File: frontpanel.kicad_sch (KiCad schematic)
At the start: 33 parts, among them J11 OLED_SOG320132A_M383, J12 Stemma-QT_QWIIC, M3 Pico_Display_Pack, Q6 Si2306BDS, SW1 STOP_SW, SW2 Rotary Enc EC11E, U10 MCP23017_SO, U14 DS3231

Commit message: More updates to regularise property names
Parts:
- BT2: Manuf (none) -> Keystone; Manuf Part No 500 -> (none); Manufacturer Keystone -> (none); Mfr Keystone Elec. -> (none); Mfr Part No 500 -> (none); Part (none) -> 500; Supl Mouser -> (none); Supl Part No 534-500 -> (none); Supl Price 1.23 -> (none); Supplier Mouser -> (none); Vendor (none) -> Mouser; Vendor Cost (none) -> 1.23; Vendor SKU (none) -> 534-500
- C24, C35, C36, C37, C38, C51: Manuf (none) -> Samsung Electro-Mechanics; Mfr Samsung Electro-Mechanics -> (none); Mfr Name C0402C104K8R7411 -> (none); Mfr Part Mouser -> (none); Mfr Part No CL21B104KACNNND -> (none); Part 0.016 -> CL21B104KACNNND; Price KEMET -> (none); Repr-Cost C0402C104K8R7411 -> (none); Stock Number Mouser -> (none); Supl Mouser -> (none); Supl Part No 187-CL21B104KACNNND -> (none); Supl Price 0.027 -> (none); Vendor (none) -> Mouser; Vendor Cost (none) -> 0.027; Vendor SKU (none) -> 187-CL21B104KACNNND
- D14: Cost 1.37 -> (none); Manuf (none) -> kingbright; Manuf Part No WP154A4SUREQBFZG -> (none); Manufacturer kingbright -> (none); Part (none) -> WP154A4SUREQBFZG; Supplier mouser -> (none); Vendor (none) -> Mouser; Vendor Cost (none) -> 1.37; Vendor SKU (none) -> WP154A4SUREQBFZG
- J11: Manuf (none) -> Surenoo; Mfr Surenoo -> (none); Mfr Part No SOG320132A_M383 -> (none); Part (none) -> SOG320132A_M383
- M3: Manuf (none) -> ThePiHut; Mfr ThePiHut -> (none)
- Q6: Manuf (none) -> Vishay; Mfr Vishay -> (none); Mfr Part No SI2306BDS-T1-E3 -> (none); Part (none) -> SI2306BDS-T1-E3; Supl Mouser -> (none); Supl Part No 781-SI2306BDS-E3 -> (none); Supl Price 0.496 -> (none); Vendor (none) -> Mouser; Vendor Cost (none) -> 0.496; Vendor SKU (none) -> 781-SI2306BDS-E3
- R23, R24, R47, R48, R49: Manuf (none) -> Yageo; Mfr Yageo -> (none); Mfr Part No RC0805FR-134K7L -> (none); Part (none) -> RC0805FR-134K7L; Supl Mouser -> (none); Supl Part No 603-RC0805FR-134K7L -> (none); Supl Price 0.077 -> (none); Vendor (none) -> Mouser; Vendor Cost (none) -> 0.077; Vendor SKU (none) -> 603-RC0805FR-134K7L
- R25, R26, R27, R28, R29: Manuf (none) -> Yageo; Mfr Yageo -> (none); Mfr Part No AC0805FR-0710KL -> (none); Part (none) -> AC0805FR-0710KL; Supl Mouser -> (none); Supl Part No 603-AC0805FR-0710KL -> (none); Supl Price 0.077 -> (none); Vendor (none) -> Mouser; Vendor Cost (none) -> 0.077; Vendor SKU (none) -> 603-AC0805FR-0710KL
- SW1: Manuf (none) -> Schurter; Mfr Schurter -> (none); Mfr Part No 1241.1082.1 -> (none); Part (none) -> 1241.1082.1; Supl Mouser -> (none); Supl Part No 693-1241.1082.1 -> (none); Supl Price 3.07 -> (none); Vendor (none) -> Mouser; Vendor Cost (none) -> 3.07; Vendor SKU (none) -> 693-1241.1082.1
- SW2: Manuf (none) -> Alps; Mfr Alps -> (none); Mfr Part No EC11E152U402 -> (none); Part (none) -> EC11E152U402; Supl Mouser -> (none); Supl Part No 688-EC11E152U402 -> (none); Supl Price 11.34 -> (none); Vendor (none) -> Mouser; Vendor Cost (none) -> 11.34; Vendor SKU (none) -> 688-EC11E152U402
- U10: Manuf (none) -> Microchip; Mfr Microchip -> (none); Mfr Part No MCP23017-E/SO -> (none); Part (none) -> MCP23017-E/SO; Supl Mouser -> (none); Supl Part No 579-MCP23017-E/SO -> (none); Supl Price 1.13 -> (none); Vendor (none) -> Mouser; Vendor Cost (none) -> 1.13; Vendor SKU (none) -> 579-MCP23017-E/SO
- U14: Manuf (none) -> Maxim; Manuf Part No DS3231S#T&R -> (none); Manufacturer Maxim Integrated -> (none); Mfr Maxim -> (none); Mfr Part No DS3231 -> (none); Part (none) -> DS3231; Stock Number 700-DS3231S#T&R- -> (none); Supplier Mouser -> (none)

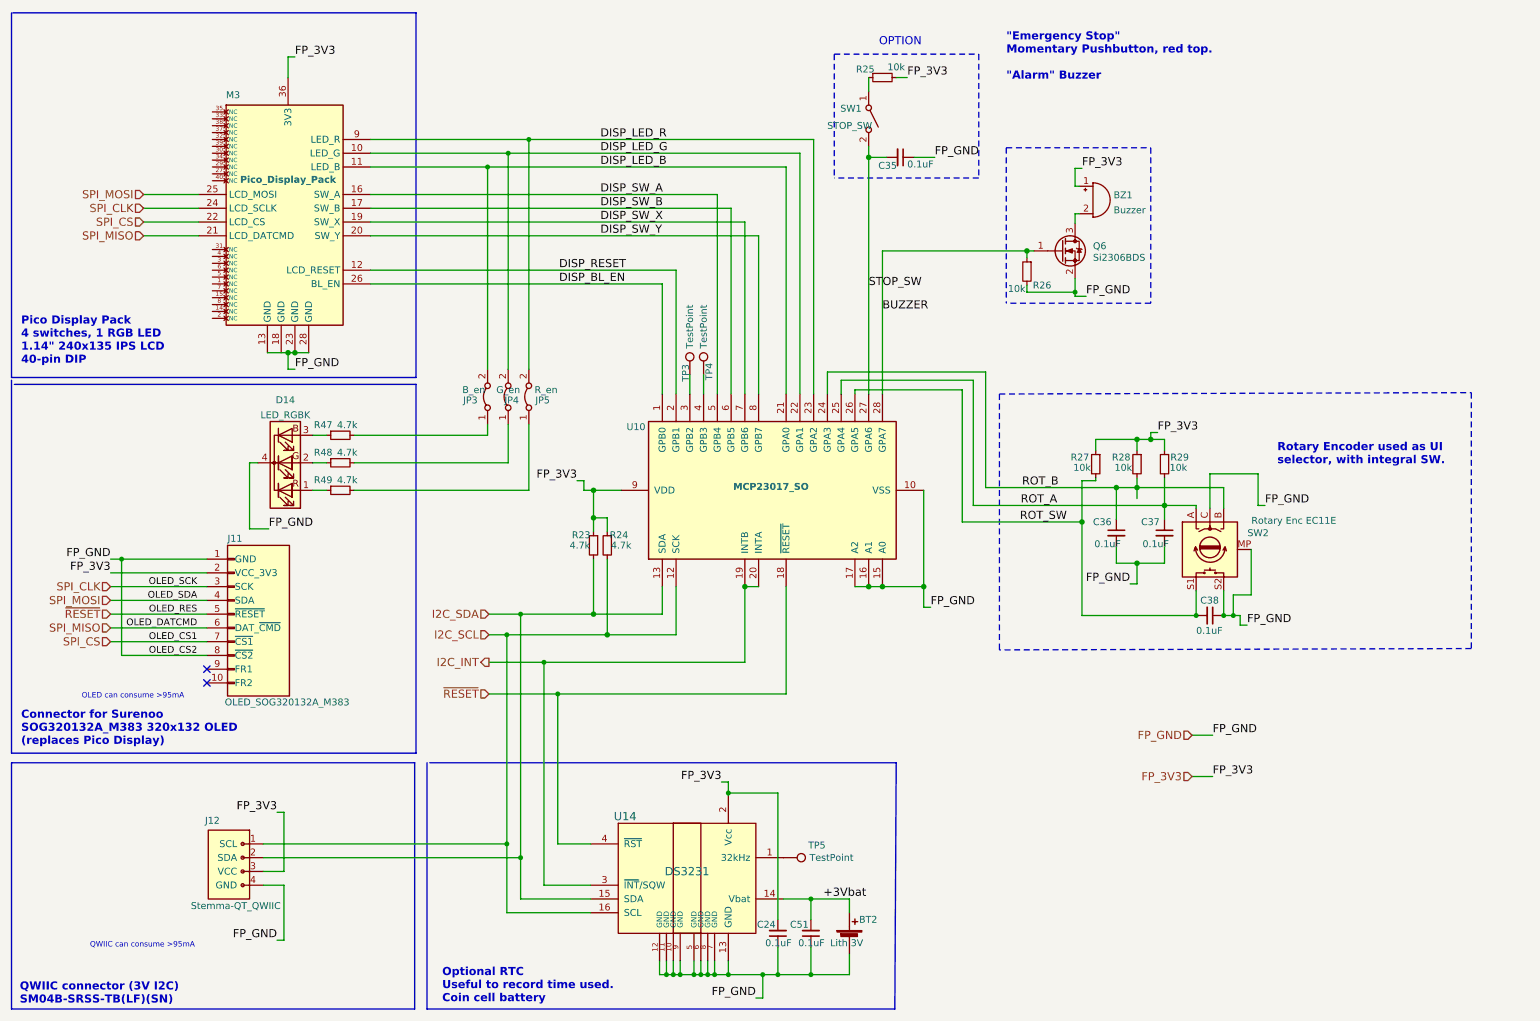
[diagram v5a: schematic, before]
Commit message: Fix some errors in the design (esp net-tie in wrong place)
 - correct led, diode footprints & model
 - fix fuse holder (bad hole spec)
 - update oled mod
 - update EC11 mod
 - add Blender models of case (xz compressed)
 - more updated gerbers (not current!)
 - improve layout of front panel pcb
 - delete unused files
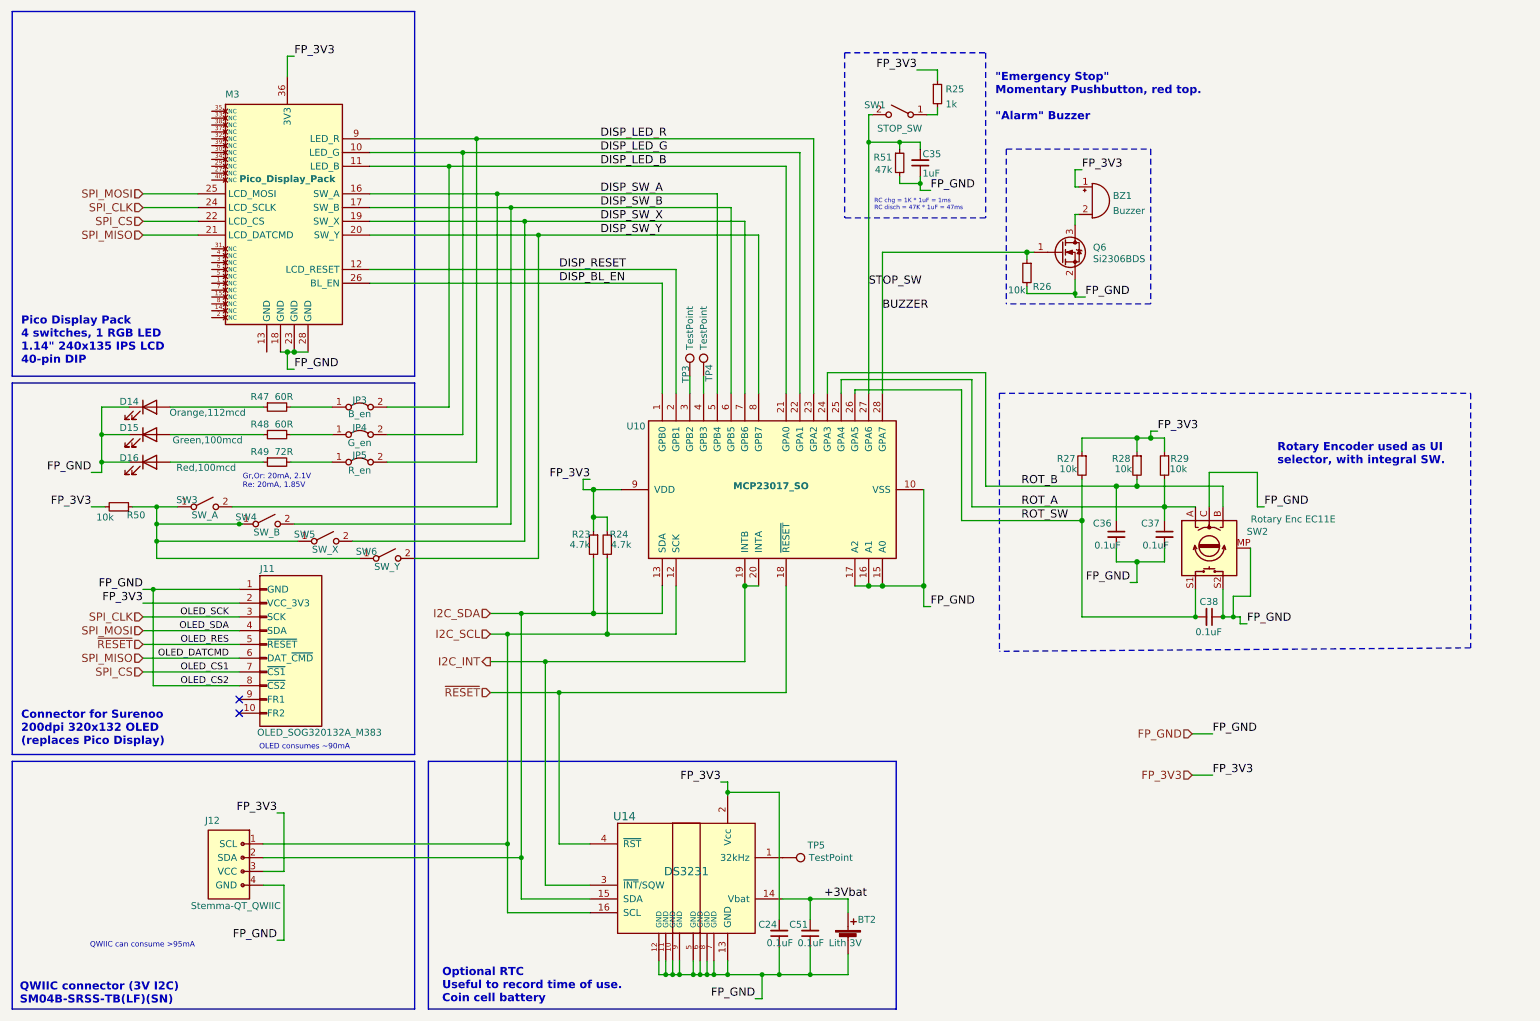
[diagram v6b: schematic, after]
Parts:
- removed D14: LED_RGBK, LED_THT:LED_D5.0mm-4_RGB_Wide_Pins, symbol Device:LED_RGBK
- added D14: Orange,112mcd, LED_SMD:LED_1206_3216Metric_Pad1.42x1.75mm_HandSolder, symbol Device:LED
- added D15: Green,100mcd, LED_SMD:LED_1210_3225Metric_Pad1.42x2.65mm_HandSolder, symbol Device:LED
- added D16: Red,100mcd, LED_SMD:LED_1206_3216Metric_Pad1.42x1.75mm_HandSolder, symbol Device:LED
- added R50: 10k, Resistor_SMD:R_0805_2012Metric_Pad1.20x1.40mm_HandSolder, symbol Device:R_Small
- added R51: 47k, Resistor_SMD:R_0805_2012Metric_Pad1.20x1.40mm_HandSolder, symbol Device:R_Small
- added SW3: SW_A, Connector_Wire:SolderWire-0.5sqmm_1x02_P4.6mm_D0.9mm_OD2.1mm, symbol Switch:SW_SPST
- added SW4: SW_B, Connector_Wire:SolderWire-0.5sqmm_1x02_P4.6mm_D0.9mm_OD2.1mm, symbol Switch:SW_SPST
- added SW5: SW_X, Connector_Wire:SolderWire-0.5sqmm_1x02_P4.6mm_D0.9mm_OD2.1mm, symbol Switch:SW_SPST
- added SW6: SW_Y, Connector_Wire:SolderWire-0.5sqmm_1x02_P4.6mm_D0.9mm_OD2.1mm, symbol Switch:SW_SPST
- C35: value 0.1uF -> 1uF; Manuf Samsung Electro-Mechanics -> Taiyo Yuden; Part CL21B104KACNNND -> EMK212BJ105KG-T; Vendor Cost 0.027 -> 0.016; Vendor SKU 187-CL21B104KACNNND -> 963-EMK212BJ105KG-T
- J11: Vendor (none) -> Surenoo; Vendor Cost (none) -> 39.95; Vendor SKU (none) -> SOG320132A_M383
- J12: Manuf (none) -> SparkFun; Part (none) -> PRT-14417; Vendor (none) -> Mouser; Vendor Cost (none) -> 0.399; Vendor SKU (none) -> 474-PRT-14417
- R25: value 10k -> 1k; Part AC0805FR-0710KL -> RC0805FR-071KL; Vendor SKU 603-AC0805FR-0710KL -> 603-RC0805FR-071KL
- R47, R48: value 4.7k -> 60R; Manuf Yageo -> Vishay / Dale; Part RC0805FR-134K7L -> CRCW080562R0JNEA; Vendor SKU 603-RC0805FR-134K7L -> 71-CRCW080562R0JNEA
- R49: value 4.7k -> 72R; Part RC0805FR-134K7L -> RC0805JR-0768RL; Vendor SKU 603-RC0805FR-134K7L -> 603-RC0805JR-0768RL
- U14: Vendor (none) -> Mouser; Vendor Cost (none) -> 7.39; Vendor SKU (none) -> 700-DS3231M+TRL
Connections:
- net DISP_SW_A: now also SW3.2 (B)
- net DISP_SW_B: now also SW4.2 (B)
- net DISP_SW_X: now also SW5.2 (B)
- net DISP_SW_Y: now also SW6.2 (B)
- net FP_3V3: now also R25.1, R50.2; no longer R25.2
- net FP_GND: now also M3.18 (GND), D14.1 (K), D15.1 (K), D16.1 (K), R51.2; no longer M3.13 (GND)
- net STOP_SW: now also R51.1
- net at R49.1: now also D16.2 (A)
- net at R47.1: now also D14.2 (A)
- net at R48.1: now also D15.2 (A)
- net at SW1.1 (A): now also R25.2; no longer R25.1
- new net: R50.1, SW3.1 (A), SW4.1 (A), SW5.1 (A), SW6.1 (A)
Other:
- note added: "Connector for Surenoo 200dpi 320x132 OLED (replaces Pico Display)"
- note added: "Gr,Or: 20mA, 2.1V Re: 20mA, 1.85V"
- note added: "OLED consumes ~90mA"
- note added: "Optional RTC Useful to record time of use. Coin cell battery"
- note added: "RC chg = 1K * 1uF = 1ms RC disch = 47K * 1uF = 47ms"
- note removed: "Connector for Surenoo SOG320132A_M383 320x132 OLED (replaces Pico Display)"
- note removed: "OLED can consume >95mA"
- note removed: "OPTION"
- note removed: "Optional RTC Useful to record time used. Coin cell battery"
- moved on the sheet: J11, JP3, JP4, JP5, R27, R47, R48, R49, SW1

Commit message: Adjust to supply 2 CS sigs to display; rename MISO to DC; larger conn cable.
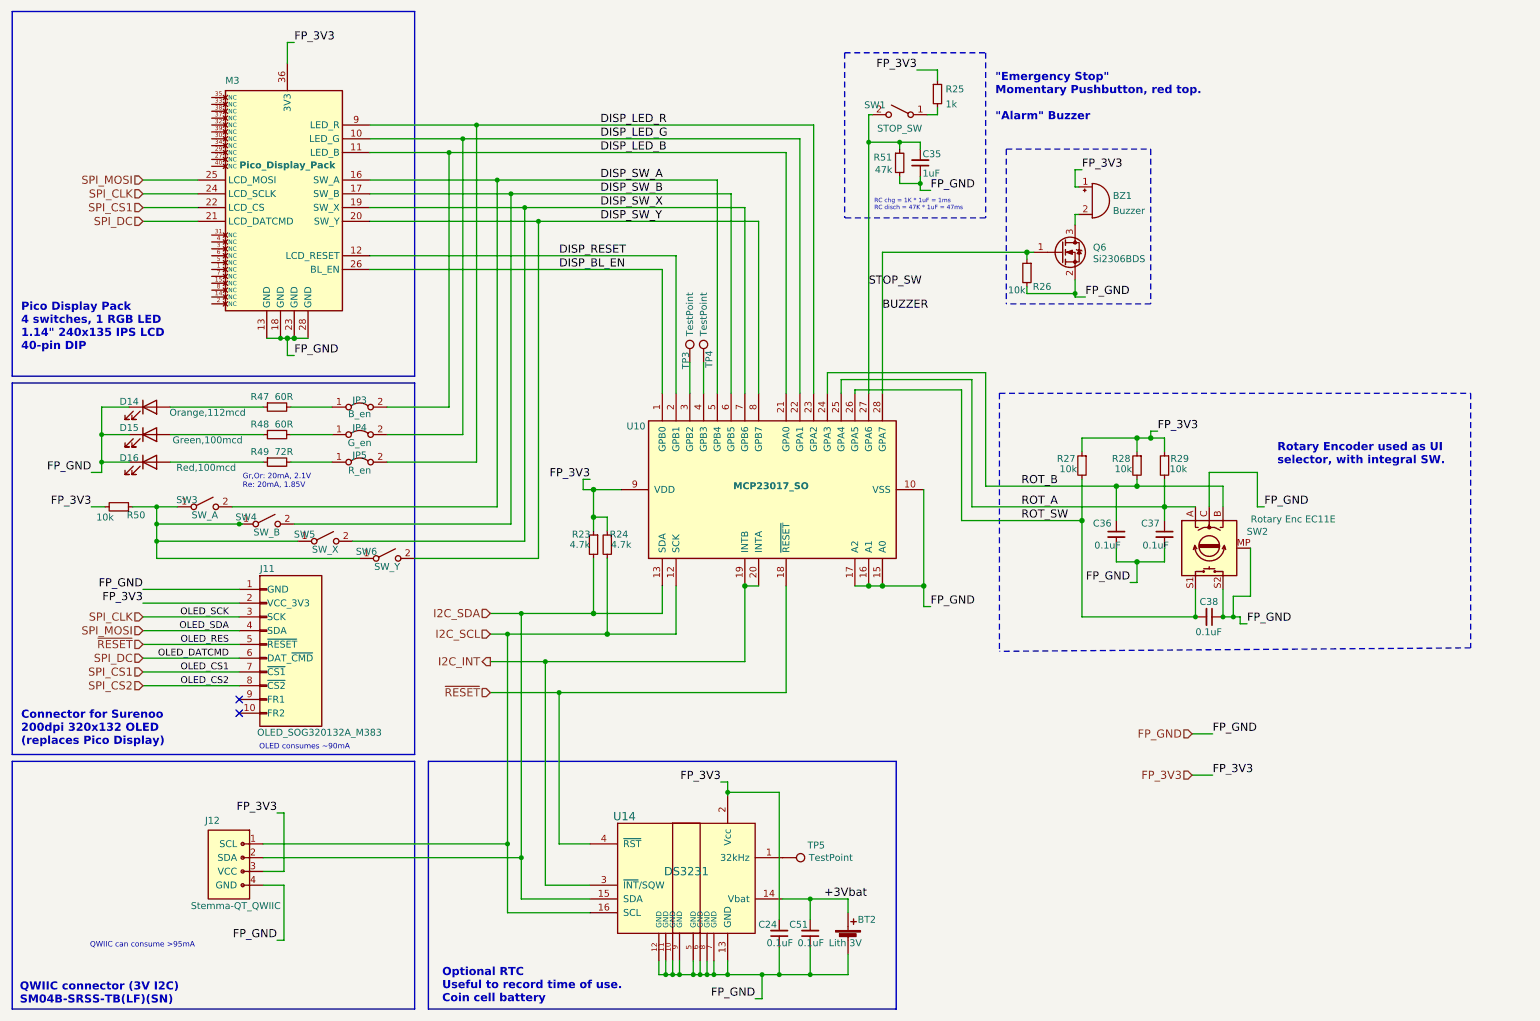
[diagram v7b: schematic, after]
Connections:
- net FP_GND: now also M3.13 (GND); no longer J11.8 (~{CS2})
- net SPI_CS renamed SPI_CS1
- net SPI_MISO renamed SPI_DC
- new net SPI_CS2: J11.8 (~{CS2})
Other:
- moved on the sheet: M3, TP3, TP4

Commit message: Lots of small changes; widen disp board to same as pwr board; use attiny mcu for rot-enc ctrl; switch to one board with cutline
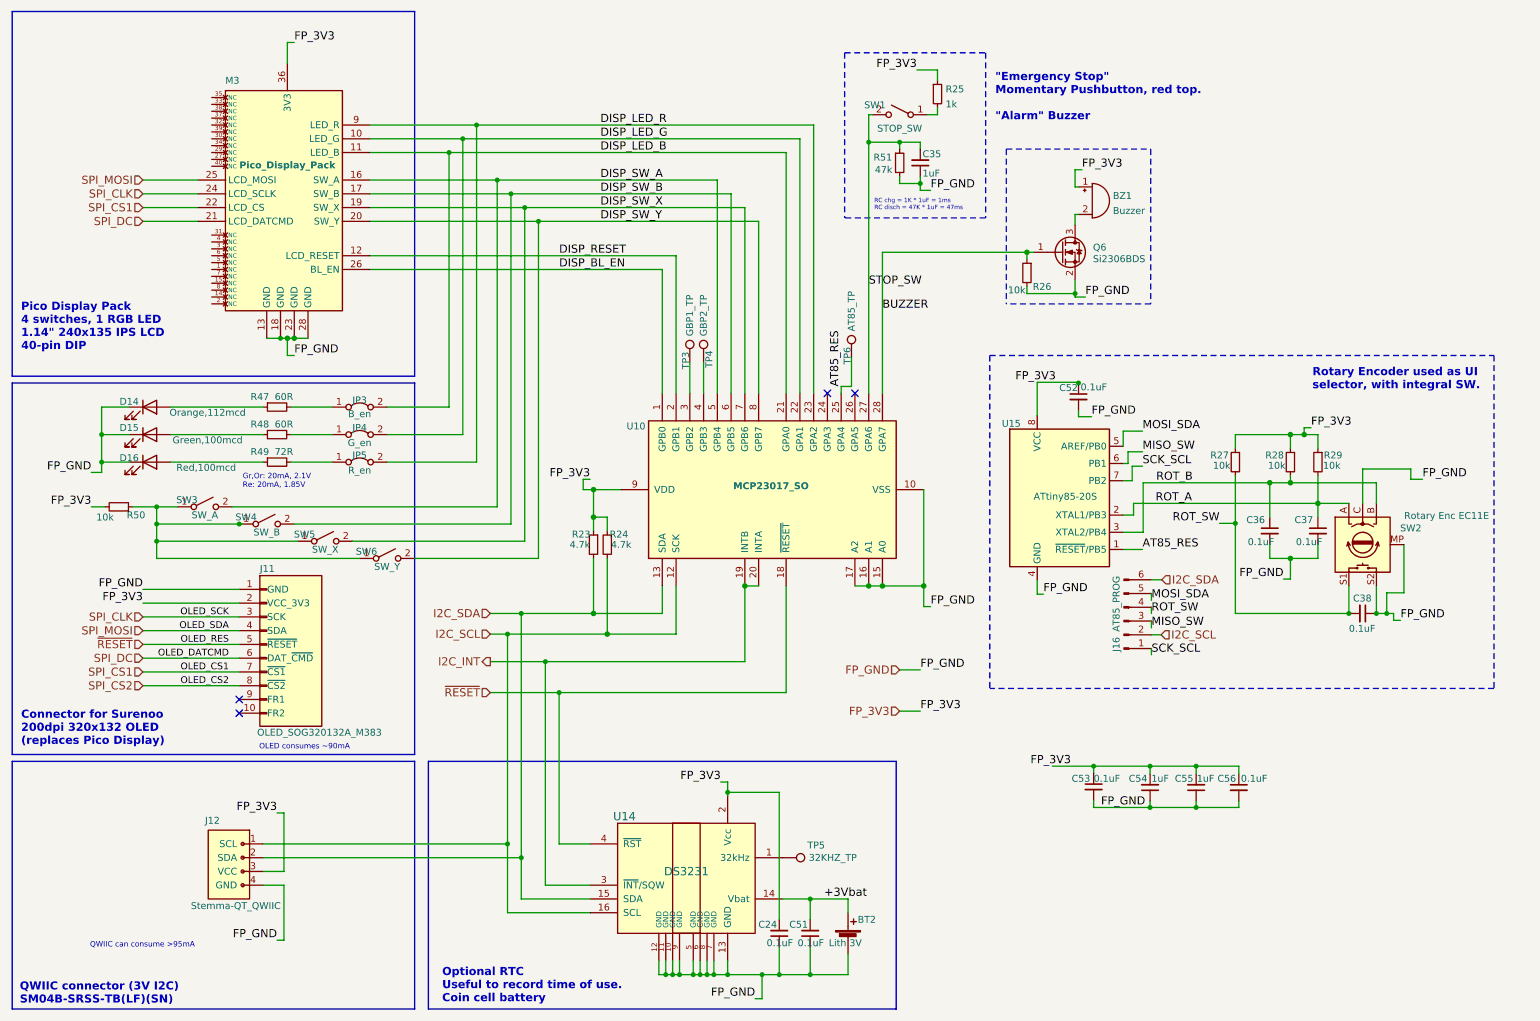
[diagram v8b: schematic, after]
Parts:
- added C52, C53, C56: 0.1uF, Capacitor_SMD:C_0805_2012Metric_Pad1.18x1.45mm_HandSolder, symbol Device:C_Small
- added C54, C55: 1uF, Capacitor_SMD:C_0805_2012Metric_Pad1.18x1.45mm_HandSolder, symbol Device:C_Small
- added J16: AT85_PROG, Connector_PinHeader_2.00mm:PinHeader_2x03_P2.00mm_Vertical, symbol Connector:Conn_01x06_Male
- added TP6: AT85_TP, TestPoint:TestPoint_Pad_1.0x1.0mm, symbol Connector:TestPoint
- added U15: ATtiny85-20S, Package_SO:SOIC-8W_5.3x5.3mm_P1.27mm, symbol MCU_Microchip_ATtiny:ATtiny85-20S
- D14: Part (none) -> 599-0230-007F
- D15: footprint LED_SMD:LED_1210_3225Metric_Pad1.42x2.65mm_HandSolder -> LED_SMD:LED_1206_3216Metric_Pad1.42x1.75mm_HandSolder
- D16: Part (none) -> APT3216SRCPRV
- M3: DNF (none) -> DNF; Part (none) -> Pico Display Pack
- TP3: value TestPoint -> GBP1_TP
- TP4: value TestPoint -> GBP2_TP
- TP5: value TestPoint -> 32KHZ_TP
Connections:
- net FP_3V3: now also C52.1, C53.1, C54.2, C55.2, C56.1, U15.8 (VCC)
- net FP_GND: now also C52.2, C53.2, C54.1, C55.1, C56.2, U15.4 (GND)
- net I2C_SCL: now also J16.2 (Pin_2)
- net I2C_SDA: now also J16.6 (Pin_6)
- net ROT_A: now also U15.2 (XTAL1/PB3); no longer U10.25 (GPA4)
- net ROT_B: now also U15.3 (XTAL2/PB4); no longer U10.24 (GPA3)
- net ROT_SW: now also J16.4 (Pin_4); no longer U10.26 (GPA5)
- new net AT85_RES: TP6.1, U10.25 (GPA4), U15.1 (~{RESET}/PB5)
- new net MISO_SW: J16.3 (Pin_3), U15.6 (PB1)
- new net MOSI_SDA: J16.5 (Pin_5), U15.5 (AREF/PB0)
- new net SCK_SCL: J16.1 (Pin_1), U15.7 (PB2)
- no-connect marks 2 -> 4
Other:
- moved on the sheet: C36, C37, C38, R27, R28, R29, SW2
